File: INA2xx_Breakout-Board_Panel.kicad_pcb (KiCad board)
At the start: 2 copper layers, 81.3 x 76.2 mm, 60 parts, among them J1 Conn_01x05_Male, J2 Conn_01x05_Male, U1 INA226

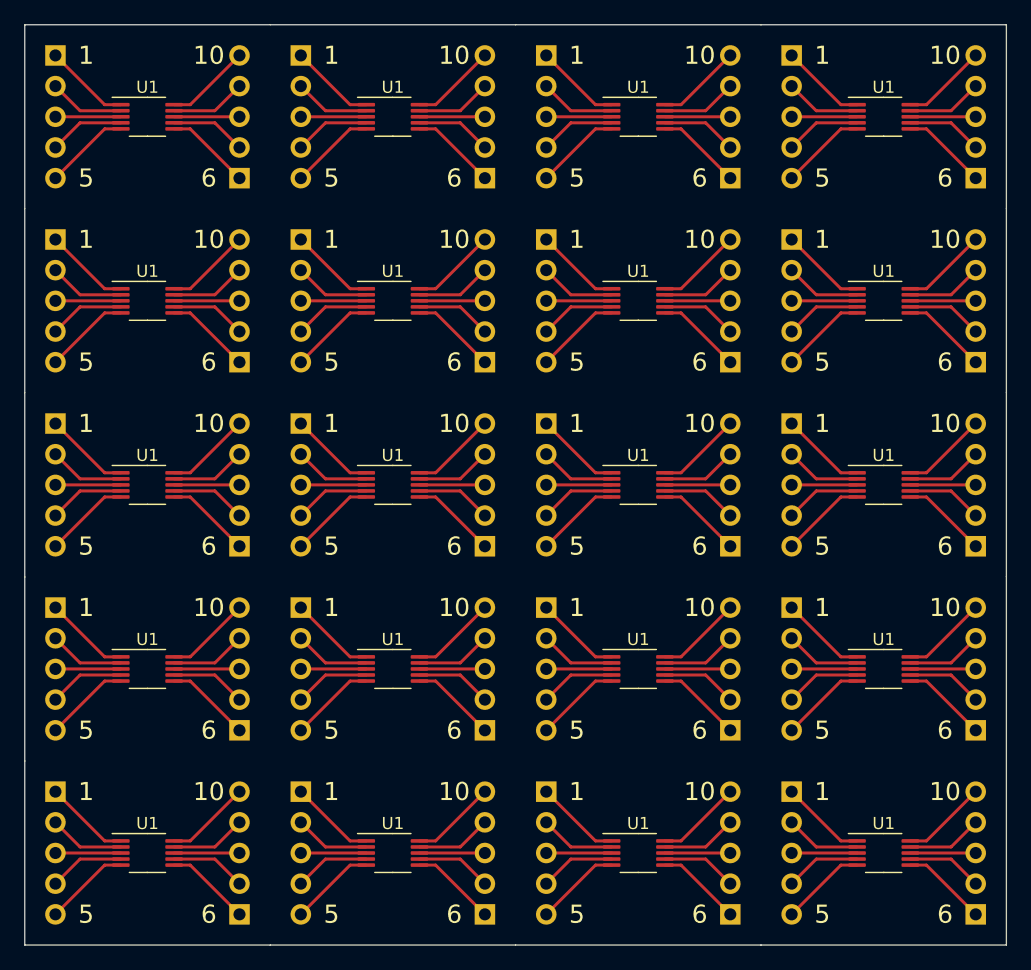
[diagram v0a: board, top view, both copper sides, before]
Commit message: Mod: Bottom filled zone, added my logo to the solder mask and exported v-cuts
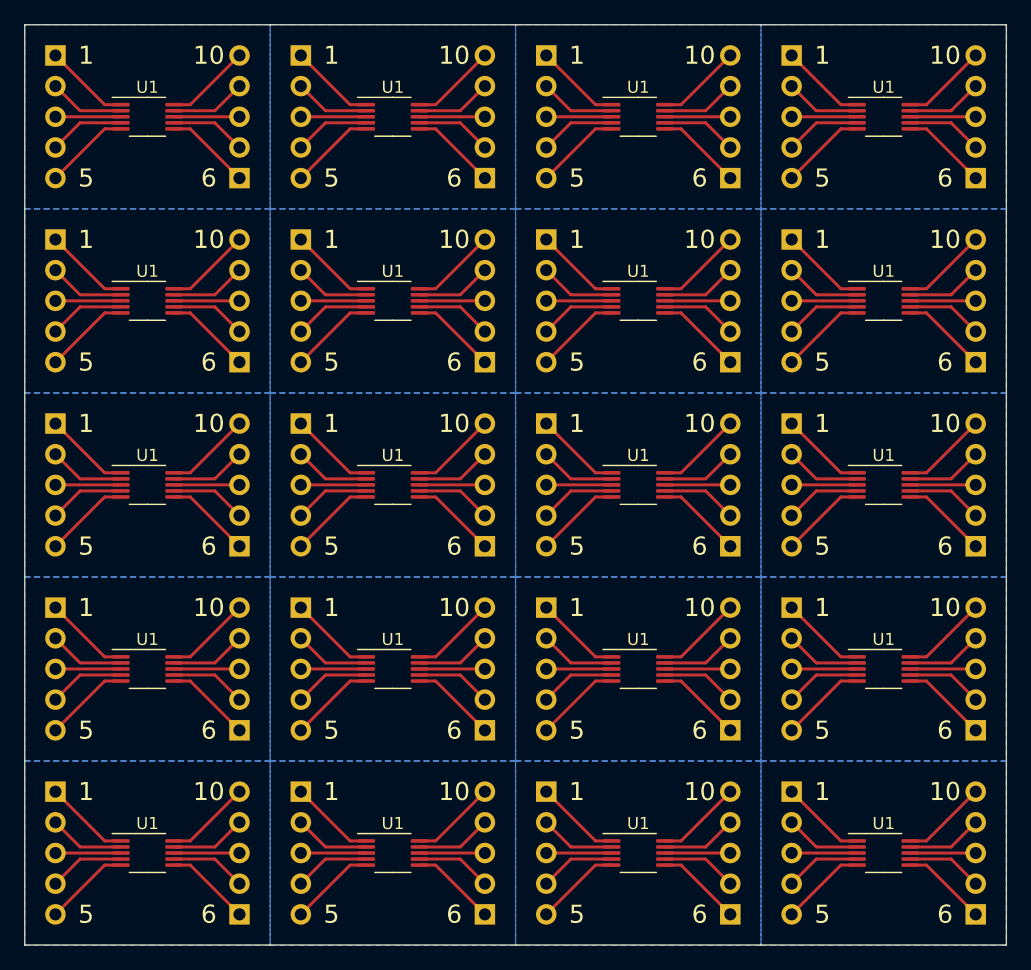
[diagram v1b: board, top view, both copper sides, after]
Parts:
- added G***: LOGO, drawings:elektronik-emblem_3x3.5_solder, B.Cu at (158.7, 68.4)
- added G***: LOGO, drawings:elektronik-emblem_3x3.5_solder, B.Cu at (138.3, 83.7)
- added G***: LOGO, drawings:elektronik-emblem_3x3.5_solder, B.Cu at (138.3, 114.1)
- added G***: LOGO, drawings:elektronik-emblem_3x3.5_solder, B.Cu at (118.0, 98.9)
- added G***: LOGO, drawings:elektronik-emblem_3x3.5_solder, B.Cu at (179.0, 83.7)
- added G***: LOGO, drawings:elektronik-emblem_3x3.5_solder, B.Cu at (138.3, 68.4)
- added G***: LOGO, drawings:elektronik-emblem_3x3.5_solder, B.Cu at (158.7, 98.9)
- added G***: LOGO, drawings:elektronik-emblem_3x3.5_solder, B.Cu at (179.0, 53.2)
- added G***: LOGO, drawings:elektronik-emblem_3x3.5_solder, B.Cu at (158.7, 83.7)
- added G***: LOGO, drawings:elektronik-emblem_3x3.5_solder, B.Cu at (179.0, 68.4)
- added G***: LOGO, drawings:elektronik-emblem_3x3.5_solder, B.Cu at (118.0, 114.1)
- added G***: LOGO, drawings:elektronik-emblem_3x3.5_solder, B.Cu at (138.3, 98.9)
- added G***: LOGO, drawings:elektronik-emblem_3x3.5_solder, B.Cu at (179.0, 98.9)
- added G***: LOGO, drawings:elektronik-emblem_3x3.5_solder, B.Cu at (138.3, 53.2)
- added G***: LOGO, drawings:elektronik-emblem_3x3.5_solder, B.Cu at (158.7, 114.1)
- added G***: LOGO, drawings:elektronik-emblem_3x3.5_solder, B.Cu at (179.0, 114.1)
- added G***: LOGO, drawings:elektronik-emblem_3x3.5_solder, B.Cu at (118.0, 53.2)
- added G***: LOGO, drawings:elektronik-emblem_3x3.5_solder, B.Cu at (158.7, 53.2)
- added G***: LOGO, drawings:elektronik-emblem_3x3.5_solder, B.Cu at (118.0, 83.7)
- added G***: LOGO, drawings:elektronik-emblem_3x3.5_solder, B.Cu at (118.0, 68.4)
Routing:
- added copper zone on B.Cu, net (none)

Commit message: Add: Project name and revision on the bottom solder mask, modified .gitignore
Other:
- board text added: "Prj: INA2xx Breakout Board Rev: A"

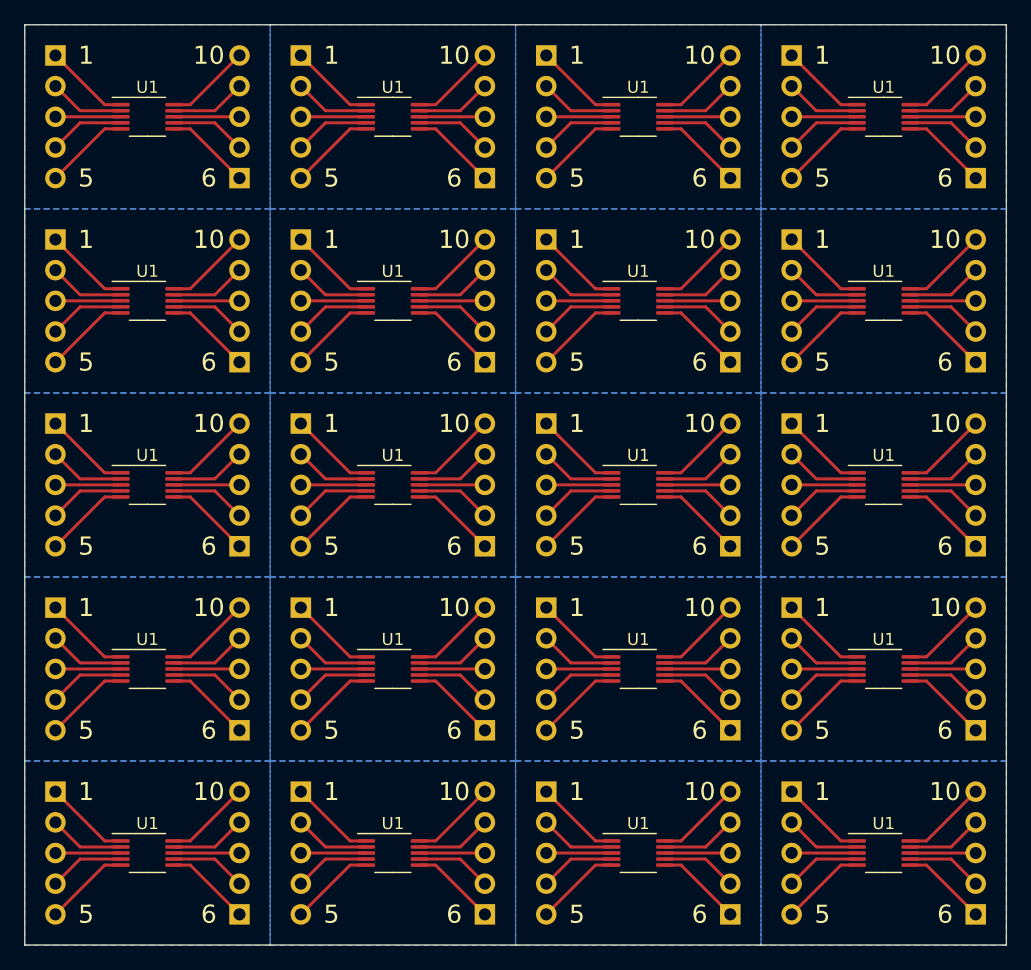
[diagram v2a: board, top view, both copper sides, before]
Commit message: Mod: Updated the project name and revision to be on the copper layer now
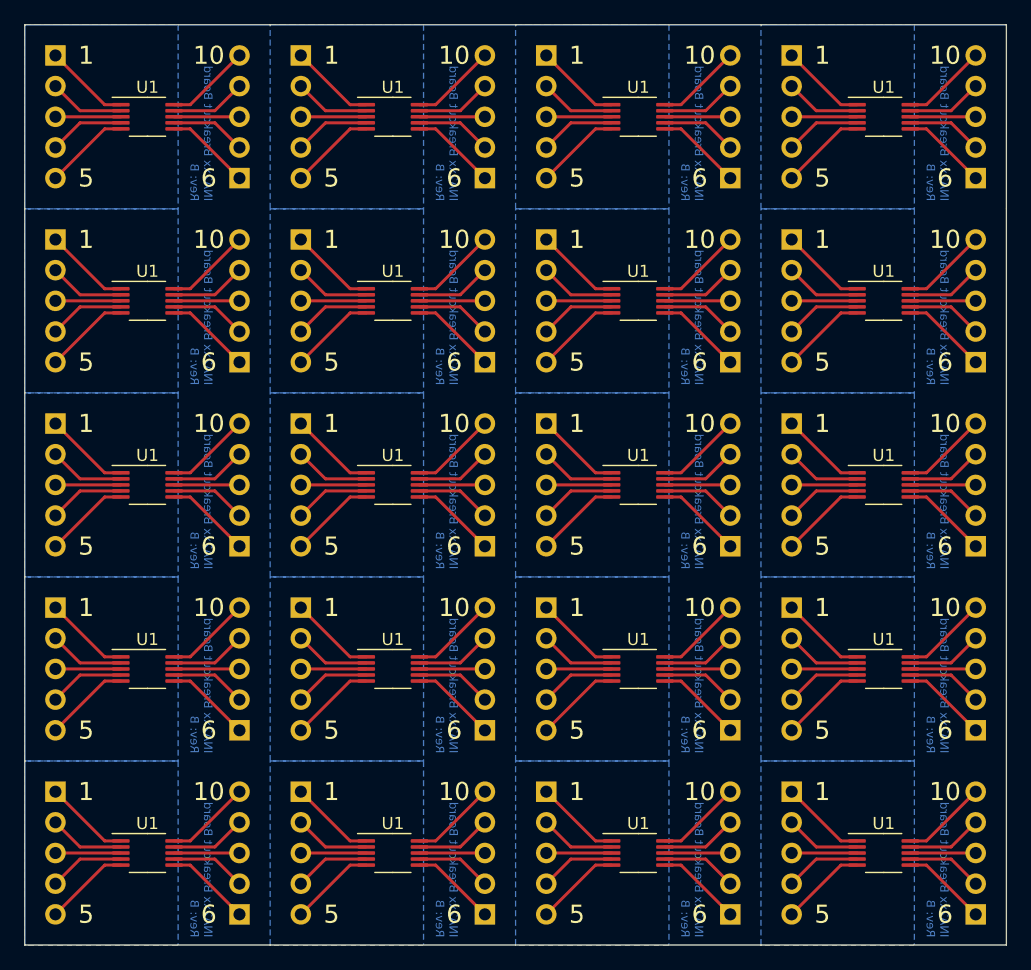
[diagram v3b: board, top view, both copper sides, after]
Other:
- board text added: "INA2xx Breakout Board Rev: B"
- board text removed: "Prj: INA2xx Breakout Board Rev: A"
